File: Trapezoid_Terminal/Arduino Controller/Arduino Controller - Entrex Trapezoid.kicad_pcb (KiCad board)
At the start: 2 copper layers, 114 x 87 mm, 18 parts, among them J1 Conn_01x19, J10 Conn_01x04, J2 Conn_01x04, J3 Conn_01x08, J4 Conn_01x08, J5 Conn_01x06, J6 Conn_01x04, J8 Conn_01x19, J9 Logic 8 CH, U1 74LS04

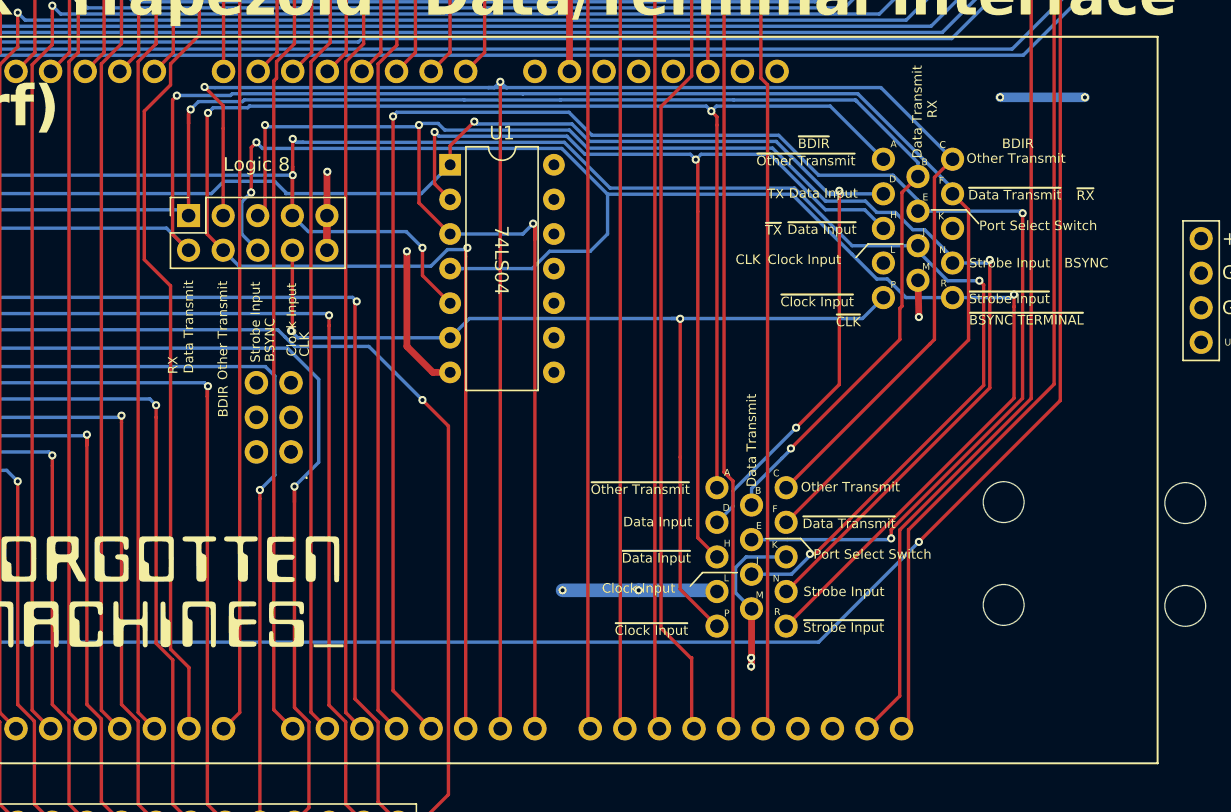
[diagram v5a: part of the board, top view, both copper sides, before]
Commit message: Trapezoid Terminal Interface Corrections
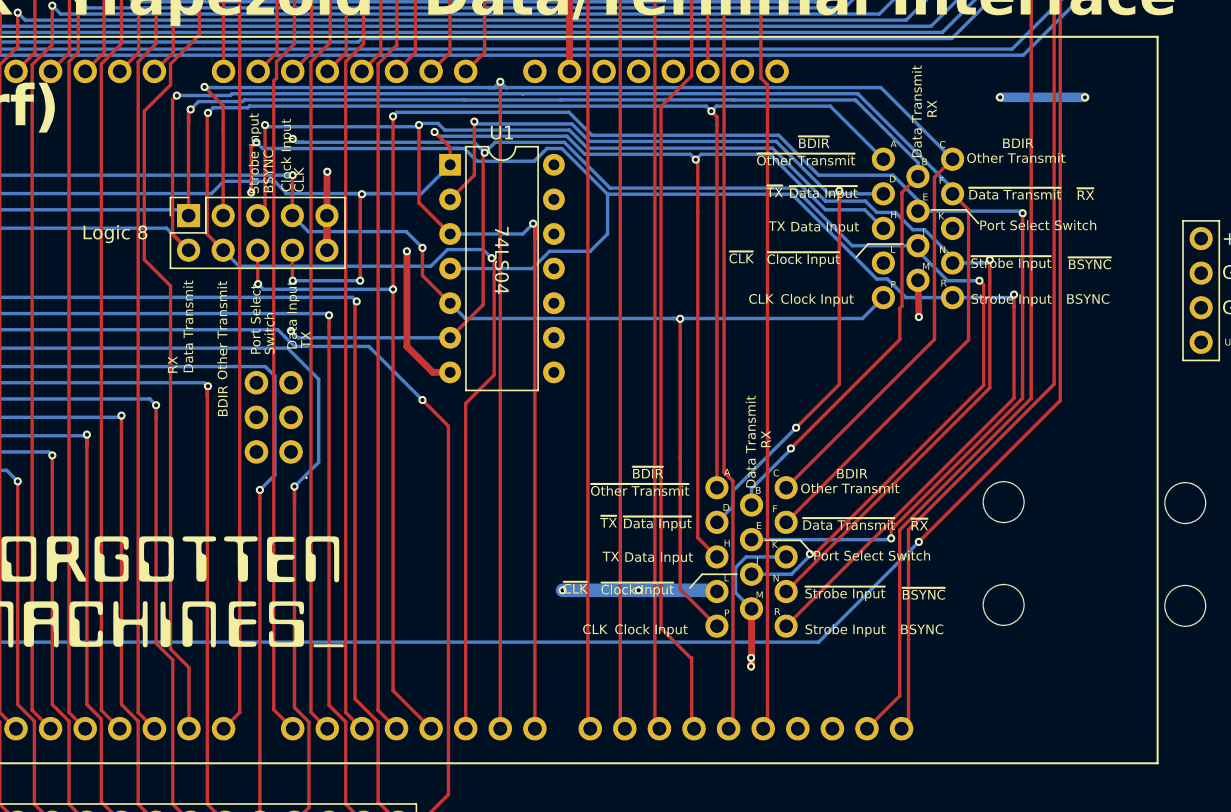
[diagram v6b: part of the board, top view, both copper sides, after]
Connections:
- J9 pad 6: ~{Strobe Input} -> Port Select Switch
- J9 pad 8: ~{Clock Input} -> Data Input
- W1 pad D: Data Input -> ~{Data Input}
- W1 pad H: ~{Data Input} -> Data Input
- W1 pad J: Clock Input -> ~{Clock Input}
- W1 pad N: Strobe Input -> ~{Strobe Input}
- W1 pad P: ~{Clock Input} -> Clock Input
- W1 pad R: ~{Strobe Input} -> Strobe Input
- W2 pad D: Data Input -> ~{Data Input}
- W2 pad H: ~{Data Input} -> Data Input
- W2 pad J: Clock Input -> ~{Clock Input}
- W2 pad N: Strobe Input -> ~{Strobe Input}
- W2 pad P: ~{Clock Input} -> Clock Input
- W2 pad R: ~{Strobe Input} -> Strobe Input
- XA1 pad VIN: +5V -> unconnected-(XA1-PadVIN)
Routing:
- net ~{Clock Input}: track 75.2 -> 113.5 mm, vias 2 -> 5
- net Clock Input: track 141.3 -> 106.2 mm, vias 5 -> 3
- net Data Input: track 112.1 -> 131.2 mm, vias 3 -> 5
- net Port Select Switch: track 134.4 -> 147.0 mm, vias 3 -> 5
- net ~{Strobe Input}: track 117.0 -> 113.3 mm
- net ~{Data Input}: track 71.5 -> 67.9 mm, vias 2 -> 3
- net ~{Other Transmit}: track 144.6 -> 146.7 mm
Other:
- board text added: "Port Select"
- board text added: "Switch"
- board text added: "~{BSYNC}"
- board text removed: "~{BSYNC TERMINAL}"
